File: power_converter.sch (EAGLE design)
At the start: 16 parts

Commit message: Completed revision 1.0
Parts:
- added C10, C11, C12, C13: 10u, rcl:C-EUC1210
- added C14, C15: 220u, LTM4607:PCR1V221MCL1GS
- added C16: 5n, rcl:C-EUC0603
- added D1: 4.7V, LTM4607:BZX84C4V7LT1G
- added JP1, JP2: (no value), pinhead-2:PINHD-1X02_2.54-SMD
- added PAD5, PAD6, PAD7, PAD8: (no value), wirepad:3,17/1,3
- added R2: 100k, rcl:R-US_R0603
- added R3: 8.5k, rcl:R-US_R0603
- added R4: 7m, rcl:R-US_R1210
- added R5: 4.7k, rcl:R-US_R0603
- added R6: 150, rcl:R-US_R0603
- added R7: 6.98k, rcl:R-US_R0603
- added R8: 2.7k, rcl:R-US_R0603
- C1, C2, C3, C5, C8, C9: value (none) -> 10u; device rcl:C-EUC1206 -> rcl:C-EUC1210
- C4: value (none) -> 10u; device Kondensatoren (rev17a):WCAP-ASLL_10X10,5_865060557008 -> rcl:C-EUC1210
- C6: value (none) -> 10u; device Kondensatoren (rev17a):WCAP-ASLI_8X10,5_865080453012 -> rcl:C-EUC1210
- C7: value (none) -> 180u; device rcl:C-EUC1206 -> LTM4607:PCR1H181MCL1GS
- L1: value (none) -> 4.7u
- PAD1, PAD2, PAD3, PAD4: device LTM4607:SMD10 -> wirepad:3,17/1,3
- R1: value (none) -> 51k; device rcl:R-US_R1210 -> rcl:R-US_R0603
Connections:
- removed net FCB: U1.FCB
- removed net STBMD: U1.STBMD
- new net N$1: R6.1, R7.2
- new net N$2: JP1.2, R1.1, R3.2
- net GND: now also C10.2, C11.2, C12.2, C13.2, C14.-, C15.-, C16.1, C7.-, D1.A, JP2.2, PAD5.P, PAD6.P, PAD7.P, PAD8.P, R3.1, R4.2, R7.1, R8.2, U1.FCB; no longer C7.2, PAD2.P, PAD4.P, R1.2
- net INTVCC: now also R2.1, R5.2
- net PGOOD: now also JP2.1, R2.2
- net PLLFLTR: now also R5.1, R8.1
- net RSENSE: now also R4.1; no longer R1.1
- net RUN: now also D1.C, JP1.1, U1.STBMD
- net SS: now also C16.2
- net VFB: now also R6.2
- net VIN: now also C1.1, C2.1, C3.1, C4.1, C7.+, PAD1.P, PAD2.P, R1.2; no longer C7.1, C9.1, PAD3.P
- net VOUT: now also C10.1, C11.1, C12.1, C13.1, C14.+, C15.+, C9.1, PAD3.P, PAD4.P; no longer C1.1, C2.1, C3.1, C4.1, PAD1.P
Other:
- note added: "Al polymer input caps: PCR1H181MCL1GS"
- note added: "Al polymer output caps: PCR1V221MCL1GS"
- note added: "Ceramic input/output caps: C3225X5R1H106K250AB"
- note added: "Examples (Rfb = R6+R7) 3.3V: Rfb = 32.4k 5V: Rfb = 19.1k 6V: Rfb = 15.4k 9V: Rfb = 9.76k 12V: Rfb = 7.15k 15V: Rfb = 5.62k 24V: Rfb = 3.4k"
- note added: "Inductor: 74439370047"
- note added: "Optocouplers recommeded for interfacing with micro-controllers"
- note added: "PGOOD is an open drain pin that is pulled to ground when output is not within 10% of regulation point. Rises to INTVCC(6V) otherwise."
- note added: "R5-R8 divider sets switching frequency to 400kHz."
- note added: "Ratings: Input voltage: 4.5V-36V Output voltage: 0.8V-24V Output current: 5A in Boost mode (Vin<Vout) 10A in Buck mode (Vin>Vout)"
- note added: "Rev: 1.0"
- note added: "Short JP1 to turn on converter."
- note added: "Two resistors can be used to set output voltage precisely. Selected values are for 12V output."
- note added: "VOUT=0.8*(100K+R6+R7)/(R6+R7)"
- note added: "V_UVLO=1.6*(R1+R3)/R3. R3 design value set higher than calculation to make 12V lock-out work in LTSpice simulation."
- moved on the sheet: C1, C2, C3, C5, C8, C9, L1, PAD1, PAD2, PAD3, PAD4, R1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

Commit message: Split current sense resistor into two; Added BOM and LTSpice simulation
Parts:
- added R9: 2.7k, rcl:R-US_R0603
- R4: value 7m -> 15m; device rcl:R-US_R1210 -> rcl:R-US_R1206
- R5: value 4.7k -> 15m; device rcl:R-US_R0603 -> rcl:R-US_R1206
- R6: value 150 -> 4.7k
- R7: value 6.98k -> 150
- R8: value 2.7k -> 6.98k
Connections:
- net GND: now also R5.2, R8.1, R9.2; no longer R7.1, R8.2
- net INTVCC: now also R6.2; no longer R5.2
- net N$1: now also R7.1, R8.2; no longer R6.1, R7.2
- net PLLFLTR: now also R6.1, R9.1; no longer R5.1, R8.1
- net RSENSE: now also R5.1
- net VFB: now also R7.2; no longer R6.2
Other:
- note added: "Examples (Rfb = R7+R8) 3.3V: Rfb = 32.4k 5V: Rfb = 19.1k 6V: Rfb = 15.4k 9V: Rfb = 9.76k 12V: Rfb = 7.15k 15V: Rfb = 5.62k 24V: Rfb = 3.4k"
- note added: "R5-R9 divider sets switching frequency to 400kHz."
- note added: "Rev: 1.1"
- note added: "VOUT=0.8*(100K+R7+R8)/(R7+R8)"
- note removed: "Examples (Rfb = R6+R7) 3.3V: Rfb = 32.4k 5V: Rfb = 19.1k 6V: Rfb = 15.4k 9V: Rfb = 9.76k 12V: Rfb = 7.15k 15V: Rfb = 5.62k 24V: Rfb = 3.4k"
- note removed: "R5-R8 divider sets switching frequency to 400kHz."
- note removed: "Rev: 1.0"
- note removed: "VOUT=0.8*(100K+R6+R7)/(R6+R7)"
- moved on the sheet: R4, R5, R6, R7, R8
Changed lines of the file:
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@@
 <part name="U1" library="LTM4607" deviceset="LTM4607EVPBF" device=""/>
 <part name="L1" library="LTM4607" deviceset="74439370047" device="" value="4.7u"/>
-<part name="R4" library="rcl" library_urn="urn:adsk.eagle:library:334" deviceset="R-US_" device="R1210" package3d_urn="urn:adsk.eagle:package:23554/2" value="7m"/>
+<part name="R5" library="rcl" library_urn="urn:adsk.eagle:library:334" deviceset="R-US_" device="R1206" package3d_urn="urn:adsk.eagle:package:23540/2" value="15m"/>
 <part name="GND7" library="supply1" library_urn="urn:adsk.eagle:library:371" deviceset="GND" device=""/>
 <part name="C8" library="rcl" library_urn="urn:adsk.eagle:library:334" deviceset="C-EU" device="C1210" package3d_urn="urn:adsk.eagle:package:23619/2" value="10u"/>
@@
 <part name="GND1" library="supply1" library_urn="urn:adsk.eagle:library:371" deviceset="GND" device=""/>
 <part name="PAD6" library="wirepad" library_urn="urn:adsk.eagle:library:412" deviceset="3,17/1,3" device="" package3d_urn="urn:adsk.eagle:package:30833/1"/>
-<part name="R6" library="rcl" library_urn="urn:adsk.eagle:library:334" deviceset="R-US_" device="R0603" package3d_urn="urn:adsk.eagle:package:23555/2" value="150"/>
+<part name="R7" library="rcl" library_urn="urn:adsk.eagle:library:334" deviceset="R-US_" device="R0603" package3d_urn="urn:adsk.eagle:package:23555/2" value="150"/>
 <part name="GND8" library="supply1" library_urn="urn:adsk.eagle:library:371" deviceset="GND" device=""/>
-<part name="R5" library="rcl" library_urn="urn:adsk.eagle:library:334" deviceset="R-US_" device="R0603" package3d_urn="urn:adsk.eagle:package:23555/2" value="4.7k"/>
-<part name="R8" library="rcl" library_urn="urn:adsk.eagle:library:334" deviceset="R-US_" device="R0603" package3d_urn="urn:adsk.eagle:package:23555/2" value="2.7k"/>
+<part name="R6" library="rcl" library_urn="urn:adsk.eagle:library:334" deviceset="R-US_" device="R0603" package3d_urn="urn:adsk.eagle:package:23555/2" value="4.7k"/>
+<part name="R9" library="rcl" library_urn="urn:adsk.eagle:library:334" deviceset="R-US_" device="R0603" package3d_urn="urn:adsk.eagle:package:23555/2" value="2.7k"/>
 <part name="C16" library="rcl" library_urn="urn:adsk.eagle:library:334" deviceset="C-EU" device="C0603" package3d_urn="urn:adsk.eagle:package:23616/2" value="5n"/>
 <part name="R2" library="rcl" library_urn="urn:adsk.eagle:library:334" deviceset="R-US_" device="R0603" package3d_urn="urn:adsk.eagle:package:23555/2" value="100k"/>
@@
 <part name="PAD7" library="wirepad" library_urn="urn:adsk.eagle:library:412" deviceset="3,17/1,3" device="" package3d_urn="urn:adsk.eagle:package:30833/1"/>
 <part name="PAD8" library="wirepad" library_urn="urn:adsk.eagle:library:412" deviceset="3,17/1,3" device="" package3d_urn="urn:adsk.eagle:package:30833/1"/>
-<part name="R7" library="rcl" library_urn="urn:adsk.eagle:library:334" deviceset="R-US_" device="R0603" package3d_urn="urn:adsk.eagle:package:23555/2" value="6.98k"/>
+<part name="R8" library="rcl" library_urn="urn:adsk.eagle:library:334" deviceset="R-US_" device="R0603" package3d_urn="urn:adsk.eagle:package:23555/2" value="6.98k"/>
 <part name="JP2" library="pinhead-2" deviceset="PINHD-1X02" device="_2.54-SMD"/>
 <part name="GND10" library="supply1" library_urn="urn:adsk.eagle:library:371" deviceset="GND" device=""/>
+<part name="R4" library="rcl" library_urn="urn:adsk.eagle:library:334" deviceset="R-US_" device="R1206" package3d_urn="urn:adsk.eagle:package:23540/2" value="15m"/>
 </parts>
 <sheets>
@@
 set output voltage precisely.
 Selected values are for 12V output.</text>
-<text x="177.8" y="73.66" size="1.778" layer="97">VOUT=0.8*(100K+R6+R7)/(R6+R7)</text>
+<text x="177.8" y="73.66" size="1.778" layer="97">VOUT=0.8*(100K+R7+R8)/(R7+R8)</text>
 <text x="25.4" y="154.94" size="1.778" layer="97">V_UVLO=1.6*(R1+R3)/R3.
 R3 design value set higher
@@
 <text x="38.1" y="139.7" size="1.778" layer="97" rot="R180">Short JP1 to
 turn on converter.</text>
-<text x="58.42" y="88.9" size="1.778" layer="97" rot="R180">R5-R8 divider sets switching
+<text x="58.42" y="88.9" size="1.778" layer="97" rot="R180">R5-R9 divider sets switching
 frequency to 400kHz.</text>
 <text x="43.18" y="48.26" size="1.778" layer="97">PGOOD is an open drain pin that
@@
 is not within 10% of regulation point.
 Rises to INTVCC(6V) otherwise.</text>
-<text x="177.8" y="68.58" size="1.778" layer="97" align="top-left">Examples (Rfb = R6+R7)
+<text x="177.8" y="68.58" size="1.778" layer="97" align="top-left">Examples (Rfb = R7+R8)
 3.3V: Rfb = 32.4k
 5V: Rfb = 19.1k
@@
 <text x="147.32" y="142.24" size="1.778" layer="97">Inductor:
 74439370047</text>
-<text x="217.17" y="20.828" size="2.1844" layer="97">Rev: 1.0</text>
+<text x="217.17" y="20.828" size="2.1844" layer="97">Rev: 1.1</text>
 </plain>
 <instances>
@@
 <instance part="U1" gate="B" x="93.98" y="137.16"/>
 <instance part="L1" gate="L" x="157.48" y="132.08" rot="R90"/>
-<instance part="R4" gate="G$1" x="154.94" y="106.68"/>
+<instance part="R5" gate="G$1" x="154.94" y="106.68"/>
 <instance part="GND7" gate="1" x="147.32" y="86.36"/>
 <instance part="C8" gate="G$1" x="167.64" y="116.84"/>
@@
 <instance part="GND1" gate="1" x="177.8" y="132.08"/>
 <instance part="PAD6" gate="1" x="162.56" y="83.82" rot="R180"/>
-<instance part="R6" gate="G$1" x="195.58" y="91.44" rot="R180"/>
+<instance part="R7" gate="G$1" x="195.58" y="91.44" rot="R180"/>
 <instance part="GND8" gate="1" x="215.9" y="86.36"/>
-<instance part="R5" gate="G$1" x="58.42" y="96.52" rot="R180"/>
-<instance part="R8" gate="G$1" x="66.04" y="86.36" rot="R270"/>
+<instance part="R6" gate="G$1" x="58.42" y="96.52" rot="R180"/>
+<instance part="R9" gate="G$1" x="66.04" y="86.36" rot="R270"/>
 <instance part="C16" gate="G$1" x="63.5" y="106.68" rot="R90"/>
 <instance part="R2" gate="G$1" x="66.04" y="127"/>
@@
 <instance part="PAD7" gate="1" x="162.56" y="76.2" rot="R180"/>
 <instance part="PAD8" gate="1" x="162.56" y="68.58" rot="R180"/>
-<instance part="R7" gate="G$1" x="208.28" y="91.44" rot="R180"/>
+<instance part="R8" gate="G$1" x="208.28" y="91.44" rot="R180"/>
 <instance part="JP2" gate="A" x="33.02" y="50.8" rot="R270"/>
 <instance part="GND10" gate="1" x="25.4" y="53.34"/>
+<instance part="R4" gate="G$1" x="154.94" y="114.3"/>
 </instances>
 <busses>
@@
 </segment>
 <segment>
-<pinref part="R5" gate="G$1" pin="2"/>
+<pinref part="R6" gate="G$1" pin="2"/>
 <wire x1="53.34" y1="96.52" x2="43.18" y2="96.52" width="0.1524" layer="91"/>
 <label x="40.64" y="96.52" size="1.778" layer="95"/>
@@
 </segment>
 <segment>
-<pinref part="R5" gate="G$1" pin="1"/>
+<pinref part="R6" gate="G$1" pin="1"/>
 <wire x1="63.5" y1="96.52" x2="66.04" y2="96.52" width="0.1524" layer="91"/>
-<pinref part="R8" gate="G$1" pin="1"/>
+<pinref part="R9" gate="G$1" pin="1"/>
 <wire x1="66.04" y1="96.52" x2="66.04" y2="91.44" width="0.1524" layer="91"/>
 <wire x1="66.04" y1="96.52" x2="73.66" y2="96.52" width="0.1524" layer="91"/>
@@
 <pinref part="U1" gate="B" pin="SENSE-"/>
 <wire x1="142.24" y1="101.6" x2="147.32" y2="101.6" width="0.1524" layer="91"/>
-<pinref part="R4" gate="G$1" pin="2"/>
+<pinref part="R5" gate="G$1" pin="2"/>
 <wire x1="147.32" y1="101.6" x2="162.56" y2="101.6" width="0.1524" layer="91"/>
 <wire x1="160.02" y1="106.68" x2="162.56" y2="106.68" width="0.1524" layer="91"/>
@@
 <junction x="154.94" y="83.82"/>
 <junction x="154.94" y="76.2"/>
+<pinref part="R4" gate="G$1" pin="2"/>
+<wire x1="160.02" y1="114.3" x2="162.56" y2="114.3" width="0.1524" layer="91"/>
+<wire x1="162.56" y1="114.3" x2="162.56" y2="106.68" width="0.1524" layer="91"/>
+<junction x="162.56" y="106.68"/>
 </segment>
 <segment>
@@
 <segment>
 <pinref part="GND8" gate="1" pin="GND"/>
-<pinref part="R7" gate="G$1" pin="1"/>
+<pinref part="R8" gate="G$1" pin="1"/>
 <wire x1="213.36" y1="91.44" x2="215.9" y2="91.44" width="0.1524" layer="91"/>
 <wire x1="215.9" y1="91.44" x2="215.9" y2="88.9" width="0.1524" layer="91"/>
@@
 </segment>
 <segment>
-<pinref part="R8" gate="G$1" pin="2"/>
+<pinref part="R9" gate="G$1" pin="2"/>
 <pinref part="GND9" gate="1" pin="GND"/>
 <wire x1="66.04" y1="81.28" x2="66.04" y2="78.74" width="0.1524" layer="91"/>
@@
 <segment>
 <pinref part="U1" gate="B" pin="VFB"/>
-<wire x1="142.24" y1="116.84" x2="147.32" y2="116.84" width="0.1524" layer="91"/>
-<label x="147.32" y="116.84" size="1.778" layer="95"/>
-</segment>
-<segment>
-<pinref part="R6" gate="G$1" pin="2"/>
+<wire x1="142.24" y1="116.84" x2="144.78" y2="116.84" width="0.1524" layer="91"/>
+<label x="144.78" y="116.84" size="1.778" layer="95"/>
+</segment>
+<segment>
+<pinref part="R7" gate="G$1" pin="2"/>
 <wire x1="190.5" y1="91.44" x2="182.88" y2="91.44" width="0.1524" layer="91"/>
 <label x="182.88" y="91.44" size="1.778" layer="95"/>
@@
 <pinref part="U1" gate="B" pin="SENSE+"/>
 <wire x1="142.24" y1="106.68" x2="147.32" y2="106.68" width="0.1524" layer="91"/>
-<pinref part="R4" gate="G$1" pin="1"/>
+<pinref part="R5" gate="G$1" pin="1"/>
 <pinref part="U1" gate="B" pin="RSENSE"/>
 <wire x1="147.32" y1="106.68" x2="149.86" y2="106.68" width="0.1524" layer="91"/>
@@
 <wire x1="147.32" y1="106.68" x2="147.32" y2="111.76" width="0.1524" layer="91"/>
 <junction x="147.32" y="106.68"/>
+<pinref part="R4" gate="G$1" pin="1"/>
+<wire x1="149.86" y1="114.3" x2="147.32" y2="114.3" width="0.1524" layer="91"/>
+<wire x1="147.32" y1="114.3" x2="147.32" y2="111.76" width="0.1524" layer="91"/>
+<junction x="147.32" y="111.76"/>
 </segment>
 </net>
@@
 <net name="N$1" class="0">
 <segment>
-<pinref part="R6" gate="G$1" pin="1"/>
-<pinref part="R7" gate="G$1" pin="2"/>
+<pinref part="R7" gate="G$1" pin="1"/>
+<pinref part="R8" gate="G$1" pin="2"/>
 <wire x1="200.66" y1="91.44" x2="203.2" y2="91.44" width="0.1524" layer="91"/>
 </segment>

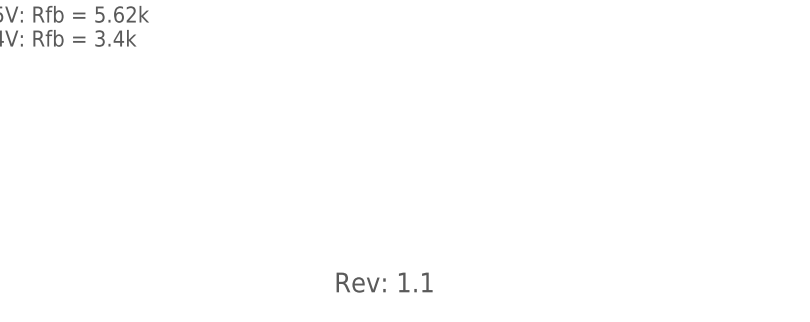
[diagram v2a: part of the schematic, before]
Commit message: Added CAM files; Increased wirepad drill; Added more vias
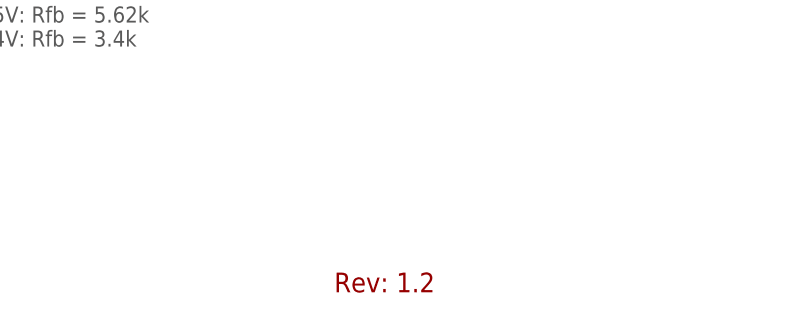
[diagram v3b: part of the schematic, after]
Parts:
- PAD1, PAD2, PAD3, PAD4, PAD5, PAD6, PAD7, PAD8: device wirepad:3,17/1,3 -> LTM4607:3,81/1,5
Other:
- note added: "Rev: 1.2"
- note removed: "Rev: 1.1"
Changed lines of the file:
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@@
 <part name="C2" library="rcl" library_urn="urn:adsk.eagle:library:334" deviceset="C-EU" device="C1210" package3d_urn="urn:adsk.eagle:package:23619/2" value="10u"/>
 <part name="C3" library="rcl" library_urn="urn:adsk.eagle:library:334" deviceset="C-EU" device="C1210" package3d_urn="urn:adsk.eagle:package:23619/2" value="10u"/>
-<part name="PAD3" library="wirepad" library_urn="urn:adsk.eagle:library:412" deviceset="3,17/1,3" device="" package3d_urn="urn:adsk.eagle:package:30833/1"/>
-<part name="PAD5" library="wirepad" library_urn="urn:adsk.eagle:library:412" deviceset="3,17/1,3" device="" package3d_urn="urn:adsk.eagle:package:30833/1"/>
+<part name="PAD3" library="LTM4607" deviceset="3,81/1,5" device="" package3d_urn="urn:adsk.eagle:package:30835/1"/>
+<part name="PAD5" library="LTM4607" deviceset="3,81/1,5" device="" package3d_urn="urn:adsk.eagle:package:30835/1"/>
 <part name="C10" library="rcl" library_urn="urn:adsk.eagle:library:334" deviceset="C-EU" device="C1210" package3d_urn="urn:adsk.eagle:package:23619/2" value="10u"/>
-<part name="PAD1" library="wirepad" library_urn="urn:adsk.eagle:library:412" deviceset="3,17/1,3" device="" package3d_urn="urn:adsk.eagle:package:30833/1"/>
+<part name="PAD1" library="LTM4607" deviceset="3,81/1,5" device="" package3d_urn="urn:adsk.eagle:package:30835/1"/>
 <part name="C1" library="rcl" library_urn="urn:adsk.eagle:library:334" deviceset="C-EU" device="C1210" package3d_urn="urn:adsk.eagle:package:23619/2" value="10u"/>
 <part name="GND1" library="supply1" library_urn="urn:adsk.eagle:library:371" deviceset="GND" device=""/>
-<part name="PAD6" library="wirepad" library_urn="urn:adsk.eagle:library:412" deviceset="3,17/1,3" device="" package3d_urn="urn:adsk.eagle:package:30833/1"/>
+<part name="PAD6" library="LTM4607" deviceset="3,81/1,5" device="" package3d_urn="urn:adsk.eagle:package:30835/1"/>
 <part name="R7" library="rcl" library_urn="urn:adsk.eagle:library:334" deviceset="R-US_" device="R0603" package3d_urn="urn:adsk.eagle:package:23555/2" value="150"/>
 <part name="GND8" library="supply1" library_urn="urn:adsk.eagle:library:371" deviceset="GND" device=""/>
@@
 <part name="C12" library="rcl" library_urn="urn:adsk.eagle:library:334" deviceset="C-EU" device="C1210" package3d_urn="urn:adsk.eagle:package:23619/2" value="10u"/>
 <part name="C13" library="rcl" library_urn="urn:adsk.eagle:library:334" deviceset="C-EU" device="C1210" package3d_urn="urn:adsk.eagle:package:23619/2" value="10u"/>
-<part name="PAD4" library="wirepad" library_urn="urn:adsk.eagle:library:412" deviceset="3,17/1,3" device="" package3d_urn="urn:adsk.eagle:package:30833/1"/>
+<part name="PAD4" library="LTM4607" deviceset="3,81/1,5" device="" package3d_urn="urn:adsk.eagle:package:30835/1"/>
 <part name="C5" library="rcl" library_urn="urn:adsk.eagle:library:334" deviceset="C-EU" device="C1210" package3d_urn="urn:adsk.eagle:package:23619/2" value="10u"/>
 <part name="C6" library="rcl" library_urn="urn:adsk.eagle:library:334" deviceset="C-EU" device="C1210" package3d_urn="urn:adsk.eagle:package:23619/2" value="10u"/>
-<part name="PAD2" library="wirepad" library_urn="urn:adsk.eagle:library:412" deviceset="3,17/1,3" device="" package3d_urn="urn:adsk.eagle:package:30833/1"/>
-<part name="PAD7" library="wirepad" library_urn="urn:adsk.eagle:library:412" deviceset="3,17/1,3" device="" package3d_urn="urn:adsk.eagle:package:30833/1"/>
-<part name="PAD8" library="wirepad" library_urn="urn:adsk.eagle:library:412" deviceset="3,17/1,3" device="" package3d_urn="urn:adsk.eagle:package:30833/1"/>
+<part name="PAD2" library="LTM4607" deviceset="3,81/1,5" device="" package3d_urn="urn:adsk.eagle:package:30835/1"/>
+<part name="PAD7" library="LTM4607" deviceset="3,81/1,5" device="" package3d_urn="urn:adsk.eagle:package:30835/1"/>
+<part name="PAD8" library="LTM4607" deviceset="3,81/1,5" device="" package3d_urn="urn:adsk.eagle:package:30835/1"/>
 <part name="R8" library="rcl" library_urn="urn:adsk.eagle:library:334" deviceset="R-US_" device="R0603" package3d_urn="urn:adsk.eagle:package:23555/2" value="6.98k"/>
 <part name="JP2" library="pinhead-2" deviceset="PINHD-1X02" device="_2.54-SMD"/>
@@
 <text x="147.32" y="142.24" size="1.778" layer="97">Inductor:
 74439370047</text>
-<text x="217.17" y="20.828" size="2.1844" layer="97">Rev: 1.1</text>
+<text x="217.17" y="20.828" size="2.1844" layer="94">Rev: 1.2</text>
 </plain>
 <instances>

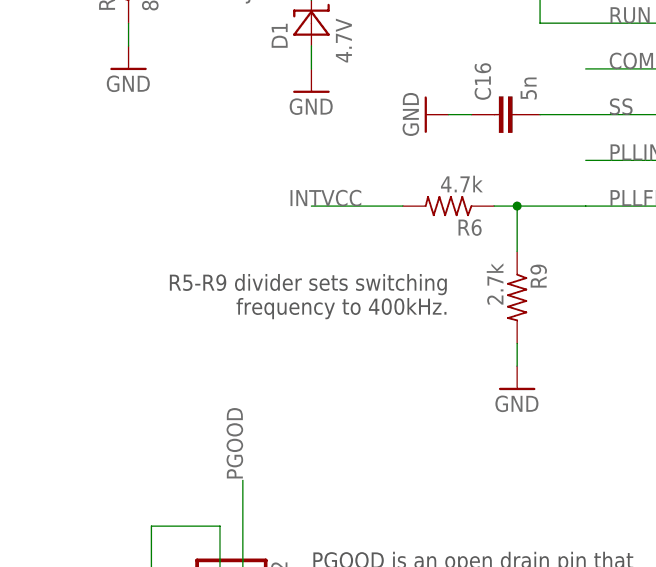
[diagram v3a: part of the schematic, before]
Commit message: fixed typo in .sch
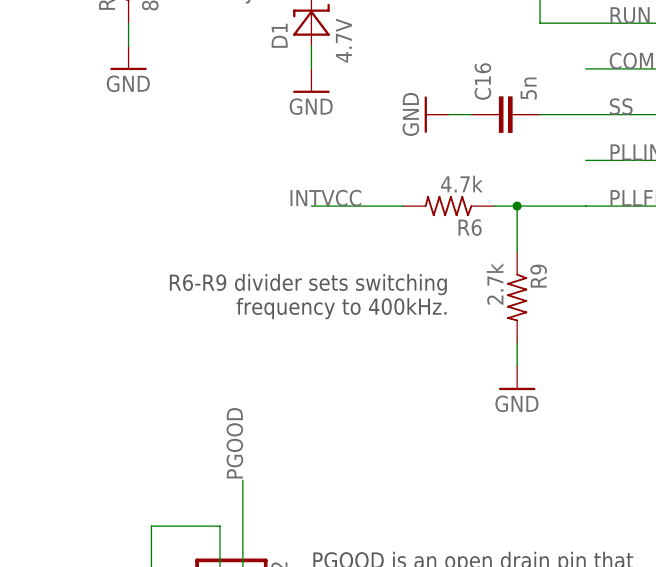
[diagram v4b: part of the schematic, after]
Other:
- note added: "R6-R9 divider sets switching frequency to 400kHz."
- note removed: "R5-R9 divider sets switching frequency to 400kHz."
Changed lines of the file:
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@@
 <text x="38.1" y="139.7" size="1.778" layer="97" rot="R180">Short JP1 to
 turn on converter.</text>
-<text x="58.42" y="88.9" size="1.778" layer="97" rot="R180">R5-R9 divider sets switching
+<text x="58.42" y="88.9" size="1.778" layer="97" rot="R180">R6-R9 divider sets switching
 frequency to 400kHz.</text>
 <text x="43.18" y="48.26" size="1.778" layer="97">PGOOD is an open drain pin that
